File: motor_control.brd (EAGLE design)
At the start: 100 x 80 mm, 13 parts, among them IC1 NE555D

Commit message: small changes
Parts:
- moved D2 30.8 mm to (14.7, 26.3), turned to 90 degrees
- moved D1 30.0 mm to (13.5, 19.0), turned to 270 degrees
- moved TP1 23.5 mm to (32.9, 23.8)
- moved C1 2.33 mm to (14.2, 13.1)
- moved R1 0.14 mm to (21.4, 28.8), turned to 270 degrees
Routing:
- net N$3: track 12.4 -> 35.4 mm
- net N$5: track 0.00 -> 9.24 mm
- net GND: track 2.41 -> 5.78 mm
- net N$9: track 0.00 -> 3.04 mm
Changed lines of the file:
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@@
 <elements>
 <element name="IC1" library="linear" package="SO08" value="NE555D" x="20.1" y="10.4" rot="R270"/>
-<element name="C1" library="rcl" package="C0805" value="2.7nF" x="15.8" y="14.8" rot="R270"/>
+<element name="C1" library="rcl" package="C0805" value="2.7nF" x="14.2" y="13.1" rot="R270"/>
 <element name="C2" library="rcl" package="C0805" value="1nF" x="28.2" y="26" rot="R270"/>
-<element name="D1" library="diode" package="SMB" value="" x="43.5" y="17.8"/>
-<element name="D2" library="diode" package="SMB" value="" x="40.3" y="9.1"/>
-<element name="R1" library="pot" package="CA6V" value="100k" x="21.3" y="28.9"/>
+<element name="D1" library="diode" package="SMB" value="" x="13.5" y="19" rot="R270"/>
+<element name="D2" library="diode" package="SMB" value="" x="14.7" y="26.3" rot="R90"/>
+<element name="R1" library="pot" package="CA6V" value="100k" x="21.4" y="28.8" rot="R270"/>
 <element name="R2" library="rcl" package="R0805" value="100" x="30.7" y="26" rot="R270"/>
 <element name="R3" library="rcl" package="R0805" value="1k" x="25.89358125" y="14.1571125" rot="R230"/>
 <element name="R4" library="rcl" package="R0805" value="1k" x="28.564278125" y="17.276603125" rot="R230"/>
 <element name="Q2" library="transistors" package="SOT-23" value="" x="29.3" y="21.6" rot="R180"/>
-<element name="TP1" library="testpad" package="B2,54" value="TPB2,54" x="11.1" y="15">
-<attribute name="TP_SIGNAL_NAME" value="" x="11.1" y="15" size="1.778" layer="27" display="off"/>
+<element name="TP1" library="testpad" package="B2,54" value="TPB2,54" x="32.9" y="23.8">
+<attribute name="TP_SIGNAL_NAME" value="" x="32.9" y="23.8" size="1.778" layer="27" display="off"/>
 </element>
 <element name="TP2" library="testpad" package="B2,54" value="TPB2,54" x="25.6" y="9.8">
@@
 <wire x1="28.3602" y1="24.8898" x2="28.2" y2="25.05" width="0.4064" layer="1"/>
 <wire x1="17.5" y1="12.305" x2="28.3602" y2="22.7014" width="0" layer="19" extent="1-1"/>
-<wire x1="15.8" y1="13.85" x2="17.5" y2="12.305" width="0" layer="19" extent="1-1"/>
+<wire x1="14.2" y1="12.15" x2="17.345" y2="12.15" width="0.4064" layer="1"/>
+<wire x1="17.345" y1="12.15" x2="17.5" y2="12.305" width="0.4064" layer="1"/>
 </signal>
 <signal name="N$3">
@@
 <contactref element="R1" pad="E"/>
 <contactref element="D1" pad="C"/>
-<wire x1="17.5" y1="11.035" x2="16.535" y2="11.035" width="0.4064" layer="1"/>
 <wire x1="16.535" y1="11.035" x2="15.9" y2="10.4" width="0.4064" layer="1"/>
 <wire x1="15.9" y1="10.4" x2="15.9" y2="8.1" width="0.4064" layer="1"/>
@@
 <wire x1="22.7" y1="9.765" x2="21.235" y2="9.765" width="0.4064" layer="1"/>
 <wire x1="21.235" y1="9.765" x2="21.2" y2="9.8" width="0.4064" layer="1"/>
-<wire x1="38.1" y1="9.1" x2="41.3" y2="17.8" width="0" layer="19" extent="1-1"/>
-<wire x1="22.7" y1="9.765" x2="38.1" y2="9.1" width="0" layer="19" extent="1-1"/>
-<wire x1="23.84" y1="26.36" x2="17.5" y2="11.035" width="0" layer="19" extent="1-1"/>
+<wire x1="13.5" y1="21.2" x2="13.5" y2="22.9" width="0.4064" layer="1"/>
+<wire x1="13.5" y1="22.9" x2="14.7" y2="24.1" width="0.4064" layer="1"/>
+<wire x1="17.5" y1="11.035" x2="16.535" y2="11.035" width="0.4064" layer="1"/>
+<wire x1="15.9" y1="10.4" x2="15.8" y2="10.3" width="0.4064" layer="1"/>
+<wire x1="15.8" y1="10.3" x2="13.3" y2="10.3" width="0.4064" layer="1"/>
+<wire x1="13.3" y1="10.3" x2="11.9" y2="11.7" width="0.4064" layer="1"/>
+<wire x1="11.9" y1="11.7" x2="11.9" y2="11.8" width="0.4064" layer="1"/>
+<wire x1="11.9" y1="11.8" x2="11.7" y2="12" width="0.4064" layer="1"/>
+<wire x1="11.7" y1="12" x2="11.7" y2="19.4" width="0.4064" layer="1"/>
+<wire x1="11.7" y1="19.4" x2="13.5" y2="21.2" width="0.4064" layer="1"/>
+<wire x1="14.7" y1="24.1" x2="18.86" y2="26.26" width="0.4064" layer="1"/>
 </signal>
 <signal name="N$4">
@@
 <contactref element="R3" pad="1"/>
 <contactref element="R2" pad="1"/>
-<wire x1="26.504228125" y1="14.884853125" x2="30.7" y2="26.95" width="0" layer="19" extent="1-1"/>
 <wire x1="17.5" y1="9.765" x2="18.865" y2="9.765" width="0.4064" layer="1"/>
 <wire x1="18.865" y1="9.765" x2="19.2" y2="10.1" width="0.4064" layer="1"/>
@@
 <wire x1="24.9" y1="15.5" x2="25.88908125" y2="15.5" width="0.4064" layer="1"/>
 <wire x1="25.88908125" y1="15.5" x2="26.504228125" y2="14.884853125" width="0.4064" layer="1"/>
+<wire x1="25.88908125" y1="15.5" x2="30.7" y2="26.95" width="0" layer="19" extent="1-1"/>
 </signal>
 <signal name="N$5">
@@
 <contactref element="D2" pad="A"/>
 <contactref element="R1" pad="S"/>
-<wire x1="22.7" y1="11.035" x2="21.3" y2="31.44" width="0" layer="19" extent="1-1"/>
-<wire x1="42.5" y1="9.1" x2="22.7" y2="11.035" width="0" layer="19" extent="1-1"/>
+<wire x1="22.7" y1="11.035" x2="14.7" y2="28.5" width="0" layer="19" extent="1-1"/>
+<wire x1="14.7" y1="28.5" x2="23.94" y2="28.8" width="0.4064" layer="1"/>
 </signal>
 <signal name="N$9">
 <contactref element="C1" pad="1"/>
 <contactref element="D1" pad="A"/>
-<wire x1="15.8" y1="15.75" x2="45.7" y2="17.8" width="0" layer="19" extent="1-1"/>
+<wire x1="14.2" y1="14.05" x2="14.2" y2="16.1" width="0.4064" layer="1"/>
+<wire x1="14.2" y1="16.1" x2="13.5" y2="16.8" width="0.4064" layer="1"/>
 </signal>
 <signal name="N$10">
 <contactref element="R1" pad="A"/>
 <contactref element="R4" pad="1"/>
-<wire x1="29.174925" y1="18.00434375" x2="29.174925" y2="18.025075" width="0.4064" layer="1"/>
-<wire x1="29.174925" y1="18.025075" x2="27.3" y2="19.9" width="0.4064" layer="1"/>
-<wire x1="27.3" y1="19.9" x2="27.3" y2="22.3" width="0.4064" layer="1"/>
-<wire x1="27.3" y1="22.3" x2="25.9" y2="23.7" width="0.4064" layer="1"/>
-<wire x1="25.9" y1="23.7" x2="25.9" y2="28.4" width="0.4064" layer="1"/>
-<wire x1="25.9" y1="28.4" x2="25.2" y2="29.1" width="0.4064" layer="1"/>
-<wire x1="25.2" y1="29.1" x2="20" y2="29.1" width="0.4064" layer="1"/>
-<wire x1="20" y1="29.1" x2="19.4" y2="28.5" width="0.4064" layer="1"/>
-<wire x1="19.4" y1="28.5" x2="19.4" y2="27" width="0.4064" layer="1"/>
-<wire x1="19.4" y1="27" x2="18.76" y2="26.36" width="0.4064" layer="1"/>
+<wire x1="18.86" y1="31.34" x2="24.76" y2="31.34" width="0.4064" layer="1"/>
+<wire x1="24.76" y1="31.34" x2="26" y2="30.1" width="0.4064" layer="1"/>
+<wire x1="26" y1="30.1" x2="26" y2="23.7" width="0.4064" layer="1"/>
+<wire x1="26" y1="23.7" x2="27.1" y2="22.6" width="0.4064" layer="1"/>
+<wire x1="27.1" y1="22.6" x2="27.1" y2="20.07926875" width="0.4064" layer="1"/>
+<wire x1="27.1" y1="20.07926875" x2="29.174925" y2="18.00434375" width="0.4064" layer="1"/>
 </signal>
 <signal name="N$6">
@@
 <wire x1="29.2746" y1="20.5332" x2="29.7668" y2="20.5332" width="0.4064" layer="1"/>
 <wire x1="29.7668" y1="20.5332" x2="31" y2="19.3" width="0.4064" layer="1"/>
-<wire x1="11.1" y1="15" x2="29.2746" y2="20.5332" width="0" layer="19" extent="1-1"/>
+<wire x1="32.9" y1="23.8" x2="29.2746" y2="20.5332" width="0" layer="19" extent="1-1"/>
 </signal>
 </signals>

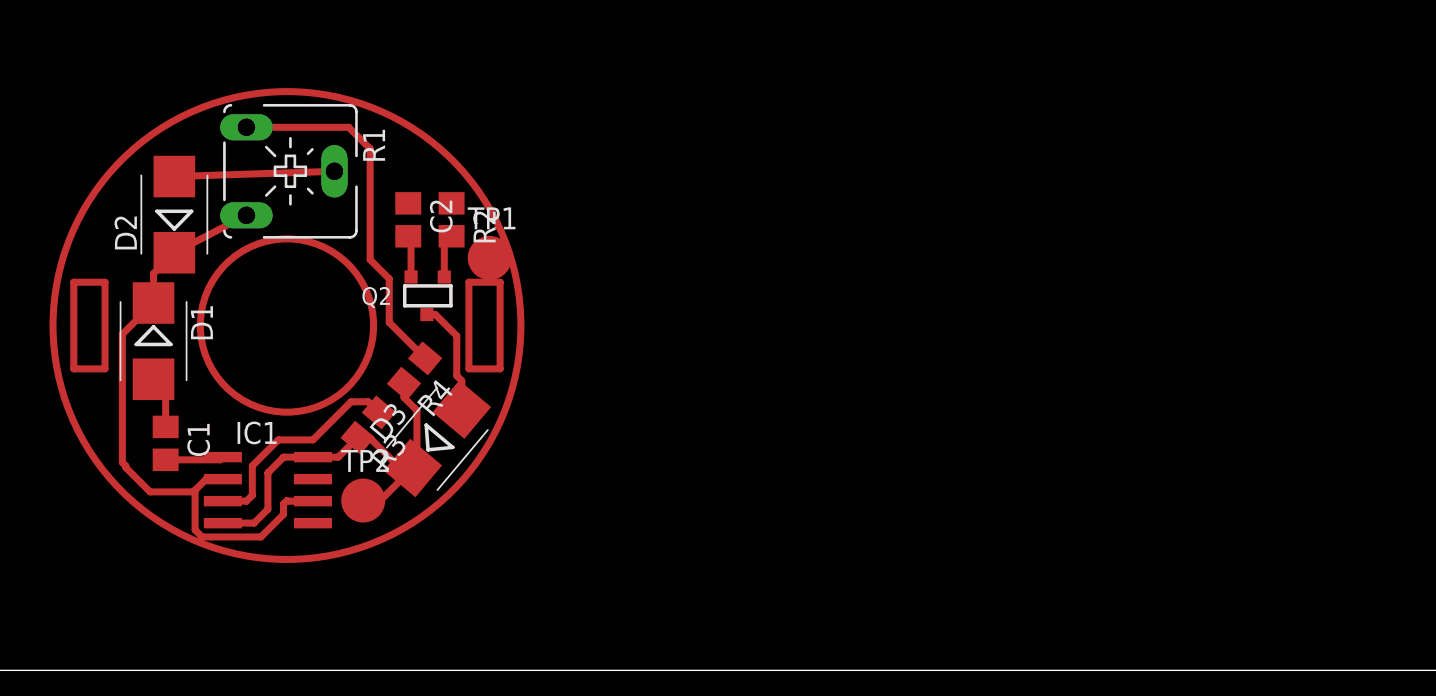
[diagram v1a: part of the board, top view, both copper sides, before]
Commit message: motor_layout first ver
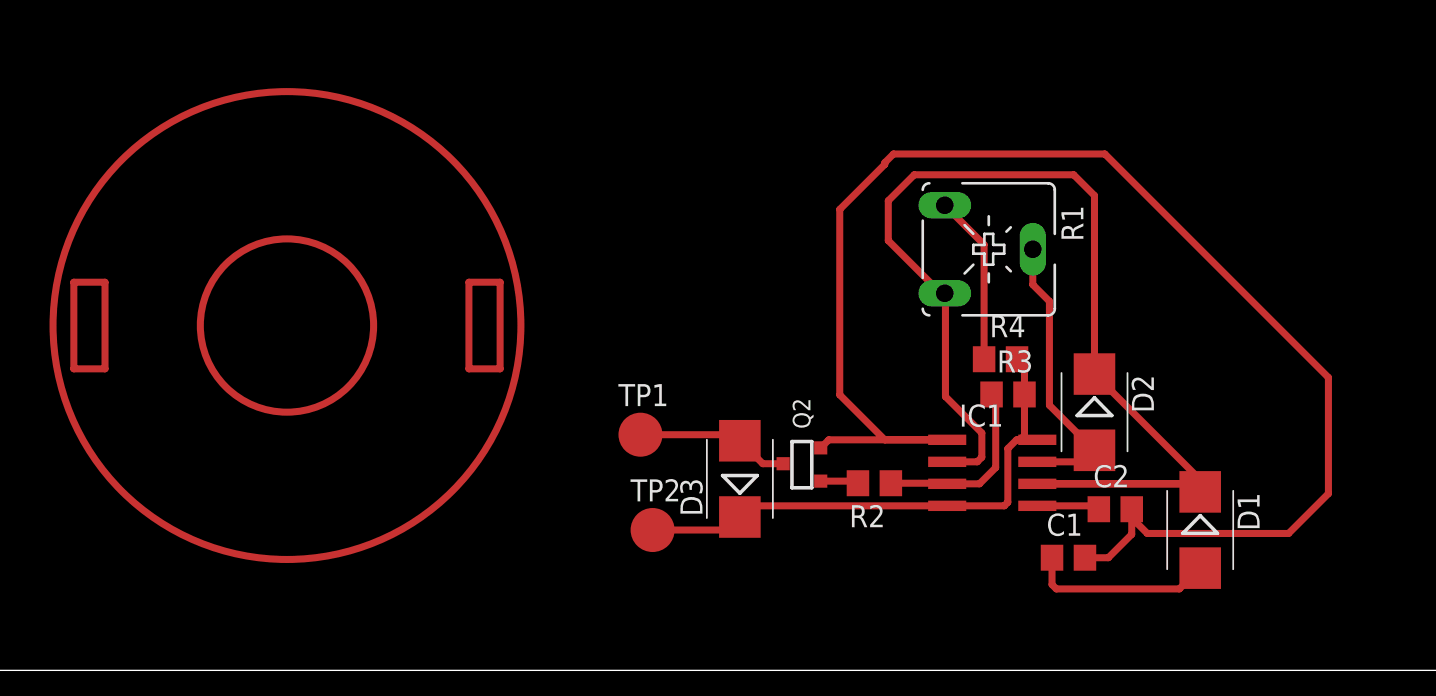
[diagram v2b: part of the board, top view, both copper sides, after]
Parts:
- moved D1 61.4 mm to (73.9, 8.10)
- moved D2 54.3 mm to (67.8, 14.9), turned to 270 degrees
- moved C1 52.5 mm to (66.3, 6.50), turned to 0 degrees
- moved C2 44.1 mm to (69.0, 9.30), turned to 0 degrees
- moved IC1 41.8 mm to (61.9, 11.4)
- moved R1 40.6 mm to (61.7, 24.3)
- moved R3 37.0 mm to (62.8, 15.9), turned to 0 degrees
- moved R4 33.8 mm to (62.4, 18.0), turned to 0 degrees
- moved R2 28.7 mm to (55.1, 10.8), turned to 180 degrees
- moved Q2 23.7 mm to (50.9, 11.9), turned to 90 degrees
- moved D3 17.6 mm to (47.3, 11.0), turned to 90 degrees
- moved TP2 16.8 mm to (42.3, 8.10)
- moved TP1 13.4 mm to (41.6, 13.6)
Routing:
- net GND: track 5.78 -> 84.5 mm
- net N$3: track 35.4 -> 71.7 mm
- net N$10: track 21.1 -> 9.82 mm
- net N$9: track 3.04 -> 10.7 mm
- net N$5: track 9.24 -> 16.7 mm
- net V+: track 24.6 -> 31.1 mm
- net N$4: track 0.00 -> 3.63 mm
- net N$8: track 6.61 -> 8.93 mm
- net N$7: track 12.6 -> 10.8 mm

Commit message: second try
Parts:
- moved C1 10.8 mm to (76.1, 11.0), turned to 270 degrees
- moved D1 5.46 mm to (73.1, 13.5), turned to 90 degrees
- moved R4 1.74 mm to (63.8, 19.0), turned to 270 degrees
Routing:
- net N$1: track 13.6 -> 0.00 mm
- net N$2: track 13.6 -> 0.00 mm
- net GND: track 84.5 -> 74.0 mm
- net N$9: track 10.7 -> 4.99 mm
- net N$3: track 71.7 -> 69.0 mm
- net N$10: track 9.82 -> 8.80 mm
- added copper zone on layer 1, net N$11
- added copper zone on layer 1, net N$12
- added copper zone on layer 1, net N$13
- added copper zone on layer 1, net N$2
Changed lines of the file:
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@@
 <wire x1="100" y1="80" x2="0" y2="80" width="0" layer="20"/>
 <wire x1="0" y1="80" x2="0" y2="0" width="0" layer="20"/>
-<circle x="21.2" y="19.9" radius="13.5" width="0.4064" layer="1"/>
-<circle x="21.2" y="19.9" radius="5" width="0.4064" layer="1"/>
 </plain>
 <attributes>
@@
 <elements>
 <element name="IC1" library="linear" package="SO08" value="NE555D" x="61.9" y="11.4" rot="R270"/>
-<element name="C1" library="rcl" package="C0805" value="2.7nF" x="66.3" y="6.5"/>
+<element name="C1" library="rcl" package="C0805" value="2.7nF" x="76.1" y="11" rot="R270"/>
 <element name="C2" library="rcl" package="C0805" value="1nF" x="69" y="9.3"/>
-<element name="D1" library="diode" package="SMB" value="" x="73.9" y="8.1" rot="R270"/>
+<element name="D1" library="diode" package="SMB" value="" x="73.1" y="13.5" rot="R90"/>
 <element name="D2" library="diode" package="SMB" value="" x="67.8" y="14.9" rot="R270"/>
 <element name="R1" library="pot" package="CA6V" value="100k" x="61.7" y="24.3" rot="R270"/>
 <element name="R2" library="rcl" package="R0805" value="100" x="55.1" y="10.8" rot="R180"/>
 <element name="R3" library="rcl" package="R0805" value="1k" x="62.810325" y="15.922140625"/>
-<element name="R4" library="rcl" package="R0805" value="1k" x="62.380003125" y="17.95595625"/>
+<element name="R4" library="rcl" package="R0805" value="1k" x="63.75595625" y="19.019996875" rot="R270"/>
 <element name="Q2" library="transistors" package="SOT-23" value="" x="50.9" y="11.9" rot="R90"/>
 <element name="TP1" library="testpad" package="B2,54" value="TPB2,54" x="41.6" y="13.6">
@@
 </elements>
 <signals>
-<signal name="N$1">
-<wire x1="33.5" y1="22.4" x2="31.7" y2="22.4" width="0.4064" layer="1"/>
-<wire x1="31.7" y1="22.4" x2="31.7" y2="17.4" width="0.4064" layer="1"/>
-<wire x1="31.7" y1="17.4" x2="33.5" y2="17.4" width="0.4064" layer="1"/>
-<wire x1="33.5" y1="17.4" x2="33.5" y2="22.4" width="0.4064" layer="1"/>
-</signal>
-<signal name="N$2">
-<wire x1="8.9" y1="22.4" x2="10.7" y2="22.4" width="0.4064" layer="1"/>
-<wire x1="10.7" y1="22.4" x2="10.7" y2="17.4" width="0.4064" layer="1"/>
-<wire x1="10.7" y1="17.4" x2="8.9" y2="17.4" width="0.4064" layer="1"/>
-<wire x1="8.9" y1="17.4" x2="8.9" y2="22.4" width="0.4064" layer="1"/>
-</signal>
 <signal name="V+">
 <contactref element="IC1" pad="8"/>
@@
 <wire x1="63.5" y1="13.3" x2="64.495" y2="13.3" width="0.4064" layer="1"/>
 <wire x1="64.495" y1="13.3" x2="64.5" y2="13.305" width="0.4064" layer="1"/>
-<wire x1="63.760325" y1="15.922140625" x2="63.760325" y2="17.525634375" width="0.4064" layer="1"/>
-<wire x1="63.760325" y1="17.525634375" x2="63.330003125" y2="17.95595625" width="0.4064" layer="1"/>
 <wire x1="63.760325" y1="15.922140625" x2="63.760325" y2="13.560325" width="0.4064" layer="1"/>
 <wire x1="63.760325" y1="13.560325" x2="63.5" y2="13.3" width="0.4064" layer="1"/>
 <wire x1="42.3" y1="8.1" x2="46.586278125" y2="8.1" width="0.4064" layer="1"/>
 <wire x1="46.586278125" y1="8.1" x2="47.33623125" y2="8.849953125" width="0.4064" layer="1"/>
+<wire x1="63.760325" y1="15.922140625" x2="63.760325" y2="18.065628125" width="0.4064" layer="1"/>
+<wire x1="63.760325" y1="18.065628125" x2="63.75595625" y2="18.069996875" width="0.4064" layer="1"/>
 </signal>
 <signal name="GND">
@@
 <wire x1="59.3" y1="13.305" x2="52.4666" y2="13.305" width="0.4064" layer="1"/>
 <wire x1="52.4666" y1="13.305" x2="52.0014" y2="12.8398" width="0.4064" layer="1"/>
-<wire x1="69.95" y1="9.3" x2="69.95" y2="8.8" width="0.4064" layer="1"/>
-<wire x1="69.95" y1="8.8" x2="69.95" y2="7.85" width="0.4064" layer="1"/>
-<wire x1="69.95" y1="7.85" x2="68.6" y2="6.5" width="0.4064" layer="1"/>
-<wire x1="68.6" y1="6.5" x2="67.25" y2="6.5" width="0.4064" layer="1"/>
 <wire x1="59.3" y1="13.305" x2="55.695" y2="13.305" width="0.4064" layer="1"/>
 <wire x1="55.695" y1="13.305" x2="53.1" y2="15.9" width="0.4064" layer="1"/>
@@
 <wire x1="55.7" y1="29.3" x2="56.2" y2="29.8" width="0.4064" layer="1"/>
 <wire x1="56.2" y1="29.8" x2="68.4" y2="29.8" width="0.4064" layer="1"/>
-<wire x1="68.4" y1="29.8" x2="81.3" y2="16.9" width="0.4064" layer="1"/>
-<wire x1="81.3" y1="16.9" x2="81.3" y2="10.2" width="0.4064" layer="1"/>
-<wire x1="81.3" y1="10.2" x2="79" y2="7.9" width="0.4064" layer="1"/>
-<wire x1="79" y1="7.9" x2="70.85" y2="7.9" width="0.4064" layer="1"/>
-<wire x1="70.85" y1="7.9" x2="69.95" y2="8.8" width="0.4064" layer="1"/>
+<wire x1="69.95" y1="9.3" x2="75.35" y2="9.3" width="0.4064" layer="1"/>
+<wire x1="75.35" y1="9.3" x2="76.1" y2="10.05" width="0.4064" layer="1"/>
+<wire x1="76.1" y1="10.05" x2="77.45" y2="10.05" width="0.4064" layer="1"/>
+<wire x1="77.45" y1="10.05" x2="78.1" y2="10.7" width="0.4064" layer="1"/>
+<wire x1="78.1" y1="10.7" x2="78.1" y2="15.7" width="0.4064" layer="1"/>
+<wire x1="78.1" y1="15.7" x2="71.3" y2="22.5" width="0.4064" layer="1"/>
+<wire x1="71.3" y1="22.5" x2="71.3" y2="26.9" width="0.4064" layer="1"/>
+<wire x1="71.3" y1="26.9" x2="68.4" y2="29.8" width="0.4064" layer="1"/>
 </signal>
 <signal name="N$3">
@@
 <wire x1="59.2" y1="15.8" x2="59.2" y2="21.72" width="0.4064" layer="1"/>
 <wire x1="59.2" y1="21.72" x2="59.16" y2="21.76" width="0.4064" layer="1"/>
-<wire x1="64.5" y1="10.765" x2="73.435" y2="10.765" width="0.4064" layer="1"/>
-<wire x1="73.435" y1="10.765" x2="73.9" y2="10.3" width="0.4064" layer="1"/>
 <wire x1="67.8" y1="17.1" x2="67.8" y2="27.4" width="0.4064" layer="1"/>
 <wire x1="67.8" y1="27.4" x2="66.6" y2="28.6" width="0.4064" layer="1"/>
@@
 <wire x1="59.4" y1="21.3" x2="59.4" y2="21.52" width="0.4064" layer="1"/>
 <wire x1="59.4" y1="21.52" x2="59.16" y2="21.76" width="0.4064" layer="1"/>
-<wire x1="64.5" y1="10.765" x2="73.935" y2="10.765" width="0.4064" layer="1"/>
-<wire x1="73.935" y1="10.765" x2="74" y2="10.7" width="0.4064" layer="1"/>
-<wire x1="74" y1="10.7" x2="74" y2="10.9" width="0.4064" layer="1"/>
-<wire x1="74" y1="10.9" x2="67.8" y2="17.1" width="0.4064" layer="1"/>
+<wire x1="64.5" y1="10.765" x2="72.565" y2="10.765" width="0.4064" layer="1"/>
+<wire x1="72.565" y1="10.765" x2="73.1" y2="11.3" width="0.4064" layer="1"/>
+<wire x1="64.5" y1="10.765" x2="72.365" y2="10.765" width="0.4064" layer="1"/>
+<wire x1="72.365" y1="10.765" x2="73" y2="11.4" width="0.4064" layer="1"/>
+<wire x1="73" y1="11.4" x2="73" y2="11.9" width="0.4064" layer="1"/>
+<wire x1="73" y1="11.9" x2="67.8" y2="17.1" width="0.4064" layer="1"/>
 </signal>
 <signal name="N$4">
@@
 <contactref element="C1" pad="1"/>
 <contactref element="D1" pad="A"/>
-<wire x1="65.35" y1="6.5" x2="65.35" y2="4.95" width="0.4064" layer="1"/>
-<wire x1="65.35" y1="4.95" x2="65.6" y2="4.7" width="0.4064" layer="1"/>
-<wire x1="65.6" y1="4.7" x2="72.7" y2="4.7" width="0.4064" layer="1"/>
-<wire x1="72.7" y1="4.7" x2="73.9" y2="5.9" width="0.4064" layer="1"/>
+<wire x1="76.1" y1="11.95" x2="76.1" y2="12.7" width="0.4064" layer="1"/>
+<wire x1="76.1" y1="12.7" x2="73.1" y2="15.7" width="0.4064" layer="1"/>
 </signal>
 <signal name="N$10">
 <contactref element="R1" pad="A"/>
 <contactref element="R4" pad="1"/>
-<wire x1="61.430003125" y1="17.95595625" x2="61.430003125" y2="24.569996875" width="0.4064" layer="1"/>
 <wire x1="61.430003125" y1="24.569996875" x2="59.16" y2="26.84" width="0.4064" layer="1"/>
+<wire x1="63.75595625" y1="19.969996875" x2="63.75595625" y2="20.64404375" width="0.4064" layer="1"/>
+<wire x1="63.75595625" y1="20.64404375" x2="61.4" y2="23" width="0.4064" layer="1"/>
+<wire x1="61.4" y1="23" x2="61.4" y2="24.53999375" width="0.4064" layer="1"/>
+<wire x1="61.4" y1="24.53999375" x2="61.430003125" y2="24.569996875" width="0.4064" layer="1"/>
 </signal>
 <signal name="N$6">
@@
 <wire x1="46.986184375" y1="13.6" x2="47.33623125" y2="13.249953125" width="0.4064" layer="1"/>
 </signal>
+<signal name="N$11">
+<polygon width="0.4064" layer="1" pour="cutout">
+<vertex x="7.7" y="19.9" curve="-180"/>
+<vertex x="34.7" y="19.9" curve="-180"/>
+</polygon>
+</signal>
+<signal name="N$12">
+<polygon width="0.4064" layer="1" pour="cutout">
+<vertex x="16.2" y="19.9" curve="-180"/>
+<vertex x="26.2" y="19.9" curve="-180"/>
+</polygon>
+</signal>
+<signal name="N$13">
+<polygon width="0.4064" layer="1" pour="cutout">
+<vertex x="8.9" y="22.4"/>
+<vertex x="10.7" y="22.4"/>
+<vertex x="10.7" y="17.4"/>
+<vertex x="8.9" y="17.4"/>
+</polygon>
+</signal>
+<signal name="N$2">
+<polygon width="0.4064" layer="1" pour="cutout">
+<vertex x="31.7" y="22.4"/>
+<vertex x="33.5" y="22.4"/>
+<vertex x="33.5" y="17.4"/>
+<vertex x="31.7" y="17.4"/>
+</polygon>
+</signal>
 </signals>

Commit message: almost done
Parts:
- moved C1 44.2 mm to (33.6, 23.3), turned to 180 degrees
- moved R4 43.0 mm to (25.8, 39.1)
- moved R3 42.7 mm to (21.0, 24.7), turned to 180 degrees
- moved D1 41.2 mm to (38.1, 35.2), turned to 180 degrees
- moved TP2 41.2 mm to (19.1, 42.1)
- moved C2 37.4 mm to (33.4, 20.6), turned to 90 degrees
- moved R2 36.6 mm to (22.7, 27.8), turned to 90 degrees
- moved IC1 35.4 mm to (27.6, 20.2)
- moved D3 34.2 mm to (23.1, 35.2), turned to 0 degrees
- moved R1 33.8 mm to (31.1, 38.6)
- moved TP1 33.4 mm to (16.2, 35.3)
- moved Q2 33.1 mm to (24.1, 31.4), turned to 0 degrees
- moved D2 30.0 mm to (39.4, 24.6), turned to 180 degrees
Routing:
- net GND: track 74.0 -> 18.5 mm
- net N$5: track 16.7 -> 28.1 mm
- net N$9: track 4.99 -> 13.4 mm
- net N$8: track 8.93 -> 3.20 mm
- net N$10: track 8.80 -> 3.25 mm
- net V+: track 31.1 -> 34.8 mm
- net N$7: track 10.8 -> 9.43 mm
- net N$3: track 69.0 -> 68.1 mm
- added copper zone on layer 1, net __
- removed copper zone on layer 1, net N$11
